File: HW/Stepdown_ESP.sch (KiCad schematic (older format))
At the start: 11 parts

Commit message: add some codes for JLCPCB, change package and schematic of CP2102
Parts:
- C? (x5): footprint Capacitor_SMD:C_1206_3216Metric -> Capacitor_SMD:C_0603_1608Metric; LCSC (none) -> C59461
- C?: LCSC (none) -> C1525
- C?: LCSC (none) -> C1567
- R?: LCSC (none) -> C25764
- U?: LCSC (none) -> C178247
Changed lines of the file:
@@
 F 0 "C?" H 4215 3646 50  0000 L CNN
 F 1 "22u" H 4215 3555 50  0000 L CNN
-F 2 "Capacitor_SMD:C_1206_3216Metric" H 4138 3450 50  0001 C CNN
+F 2 "Capacitor_SMD:C_0603_1608Metric" H 4138 3450 50  0001 C CNN
 F 3 "~" H 4100 3600 50  0001 C CNN
+F 4 "C59461" H 4100 3600 50  0001 C CNN "LCSC"
 	1    4100 3600
 	1    0    0    -1
@@
 F 0 "C?" H 4665 3646 50  0000 L CNN
 F 1 "22u" H 4665 3555 50  0000 L CNN
-F 2 "Capacitor_SMD:C_1206_3216Metric" H 4588 3450 50  0001 C CNN
+F 2 "Capacitor_SMD:C_0603_1608Metric" H 4588 3450 50  0001 C CNN
 F 3 "~" H 4550 3600 50  0001 C CNN
+F 4 "C59461" H 4550 3600 50  0001 C CNN "LCSC"
 	1    4550 3600
 	1    0    0    -1
@@
 F 0 "C?" H 5115 3646 50  0000 L CNN
 F 1 "22u" H 5115 3555 50  0000 L CNN
-F 2 "Capacitor_SMD:C_1206_3216Metric" H 5038 3450 50  0001 C CNN
+F 2 "Capacitor_SMD:C_0603_1608Metric" H 5038 3450 50  0001 C CNN
 F 3 "~" H 5000 3600 50  0001 C CNN
+F 4 "C59461" H 5000 3600 50  0001 C CNN "LCSC"
 	1    5000 3600
 	1    0    0    -1
@@
 F 2 "Resistor_SMD:R_0402_1005Metric" V 7380 3500 50  0001 C CNN
 F 3 "~" H 7450 3500 50  0001 C CNN
+F 4 "C25764" H 7450 3500 50  0001 C CNN "LCSC"
 	1    7450 3500
 	1    0    0    -1
@@
 F 2 "Capacitor_SMD:C_0402_1005Metric" H 6688 2750 50  0001 C CNN
 F 3 "~" H 6650 2900 50  0001 C CNN
+F 4 "C1525" H 6650 2900 50  0001 C CNN "LCSC"
 	1    6650 2900
 	0    1    1    0
@@
 F 2 "Capacitor_SMD:C_0402_1005Metric" H 8238 3400 50  0001 C CNN
 F 3 "~" H 8200 3550 50  0001 C CNN
+F 4 "C1567" H 8200 3550 50  0001 C CNN "LCSC"
 	1    8200 3550
 	-1   0    0    1
@@
 F 0 "C?" H 8585 3504 50  0000 R CNN
 F 1 "22u" H 8585 3595 50  0000 R CNN
-F 2 "Capacitor_SMD:C_1206_3216Metric" H 8738 3400 50  0001 C CNN
+F 2 "Capacitor_SMD:C_0603_1608Metric" H 8738 3400 50  0001 C CNN
 F 3 "~" H 8700 3550 50  0001 C CNN
+F 4 "C59461" H 8700 3550 50  0001 C CNN "LCSC"
 	1    8700 3550
 	-1   0    0    1
@@
 F 0 "C?" H 8935 3504 50  0000 R CNN
 F 1 "22u" H 8935 3595 50  0000 R CNN
-F 2 "Capacitor_SMD:C_1206_3216Metric" H 9088 3400 50  0001 C CNN
+F 2 "Capacitor_SMD:C_0603_1608Metric" H 9088 3400 50  0001 C CNN
 F 3 "~" H 9050 3550 50  0001 C CNN
+F 4 "C59461" H 9050 3550 50  0001 C CNN "LCSC"
 	1    9050 3550
 	-1   0    0    1
@@
 F 2 "Package_TO_SOT_SMD:TSOT-23-6" H 7050 3250 50  0001 C CNN
 F 3 "" H 6350 3600 50  0001 C CNN
+F 4 "C178247" H 6350 3600 50  0001 C CNN "LCSC"
 	1    6350 3600
 	1    0    0    -1

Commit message: add footprint of inductor, add codes for JLCPCB, repair mistakes
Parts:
- L?: footprint Inductor_SMD:L_0603_1608Metric -> my_library:MWSA0503S; LCSC (none) -> C408410
- R?: LCSC (none) -> C25895
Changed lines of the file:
@@
 F 2 "Resistor_SMD:R_0402_1005Metric" V 7380 4050 50  0001 C CNN
 F 3 "~" H 7450 4050 50  0001 C CNN
+F 4 "C25895" H 7450 4050 50  0001 C CNN "LCSC"
 	1    7450 4050
 	1    0    0    -1
@@
 F 0 "L?" V 7290 3300 50  0000 C CNN
 F 1 "4u7" V 7199 3300 50  0000 C CNN
-F 2 "Inductor_SMD:L_0603_1608Metric" H 7100 3300 50  0001 C CNN
+F 2 "my_library:MWSA0503S" H 7100 3300 50  0001 C CNN
 F 3 "~" H 7100 3300 50  0001 C CNN
+F 4 "C408410" H 7100 3300 50  0001 C CNN "LCSC"
 	1    7100 3300
 	0    -1   -1   0

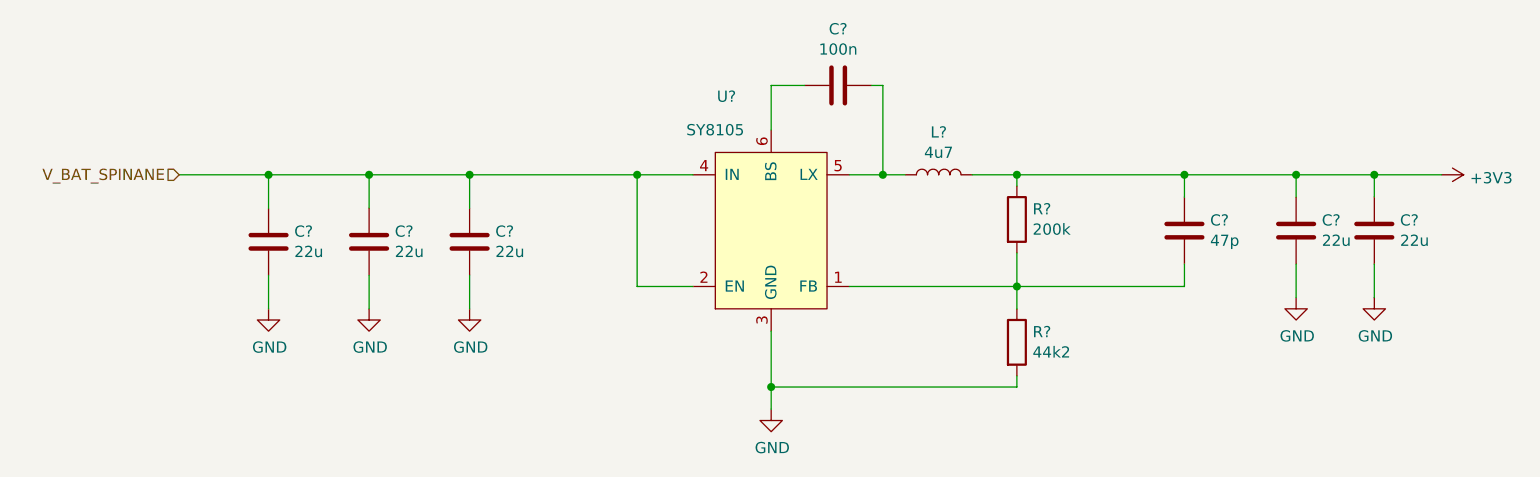
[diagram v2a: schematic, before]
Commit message: numbering components, place components on board
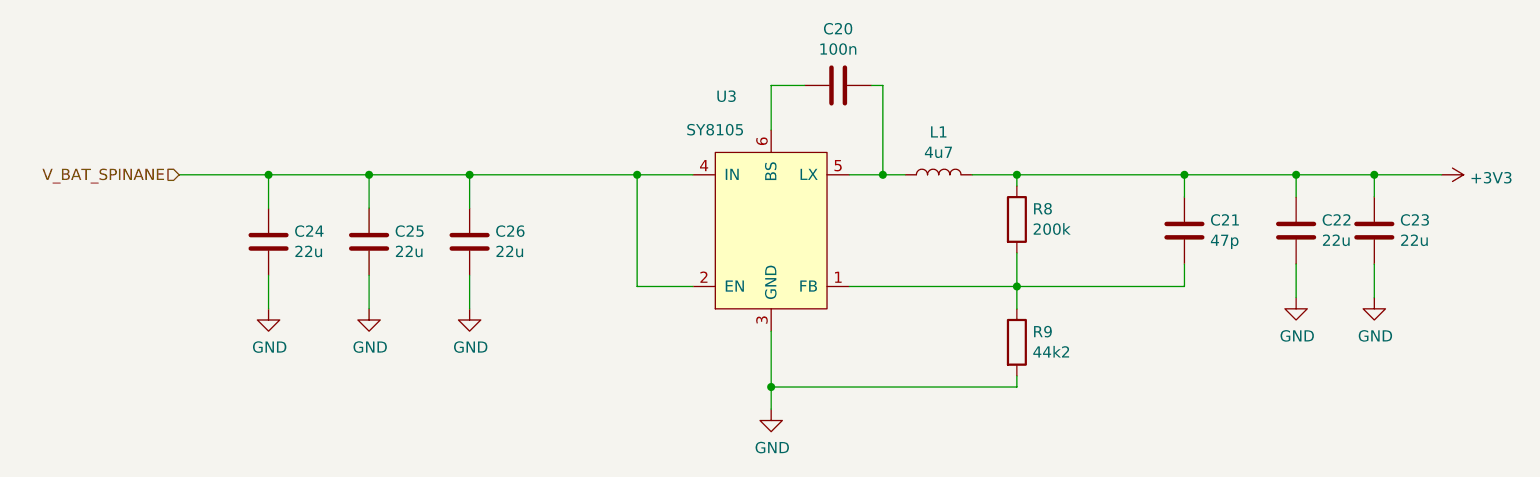
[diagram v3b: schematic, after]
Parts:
- gave numbers to parts that had none: 11
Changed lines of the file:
@@
 $EndDescr
 $Comp
-L Device:C C?
+L Device:C C24
 U 1 1 602B6CC6
 P 4100 3600
-F 0 "C?" H 4215 3646 50  0000 L CNN
+F 0 "C24" H 4215 3646 50  0000 L CNN
 F 1 "22u" H 4215 3555 50  0000 L CNN
 F 2 "Capacitor_SMD:C_0603_1608Metric" H 4138 3450 50  0001 C CNN
@@
 $EndComp
 $Comp
-L Device:C C?
+L Device:C C25
 U 1 1 602B7EED
 P 4550 3600
-F 0 "C?" H 4665 3646 50  0000 L CNN
+F 0 "C25" H 4665 3646 50  0000 L CNN
 F 1 "22u" H 4665 3555 50  0000 L CNN
 F 2 "Capacitor_SMD:C_0603_1608Metric" H 4588 3450 50  0001 C CNN
@@
 $EndComp
 $Comp
-L Device:C C?
+L Device:C C26
 U 1 1 602B82B1
 P 5000 3600
-F 0 "C?" H 5115 3646 50  0000 L CNN
+F 0 "C26" H 5115 3646 50  0000 L CNN
 F 1 "22u" H 5115 3555 50  0000 L CNN
 F 2 "Capacitor_SMD:C_0603_1608Metric" H 5038 3450 50  0001 C CNN
@@
 $EndComp
 $Comp
-L power:GND #PWR?
+L power:GND #PWR0133
 U 1 1 602B858C
 P 4100 3900
-F 0 "#PWR?" H 4100 3650 50  0001 C CNN
+F 0 "#PWR0133" H 4100 3650 50  0001 C CNN
 F 1 "GND" H 4105 3727 50  0000 C CNN
 F 2 "" H 4100 3900 50  0001 C CNN
@@
 $EndComp
 $Comp
-L power:GND #PWR?
+L power:GND #PWR0134
 U 1 1 602B8981
 P 4550 3900
-F 0 "#PWR?" H 4550 3650 50  0001 C CNN
+F 0 "#PWR0134" H 4550 3650 50  0001 C CNN
 F 1 "GND" H 4555 3727 50  0000 C CNN
 F 2 "" H 4550 3900 50  0001 C CNN
@@
 $EndComp
 $Comp
-L power:GND #PWR?
+L power:GND #PWR0135
 U 1 1 602B8C3F
 P 5000 3900
-F 0 "#PWR?" H 5000 3650 50  0001 C CNN
+F 0 "#PWR0135" H 5000 3650 50  0001 C CNN
 F 1 "GND" H 5005 3727 50  0000 C CNN
 F 2 "" H 5000 3900 50  0001 C CNN
@@
 Connection ~ 5000 3300
 $Comp
-L Device:R R?
+L Device:R R8
 U 1 1 602BA607
 P 7450 3500
-F 0 "R?" H 7520 3546 50  0000 L CNN
+F 0 "R8" H 7520 3546 50  0000 L CNN
 F 1 "200k" H 7520 3455 50  0000 L CNN
 F 2 "Resistor_SMD:R_0402_1005Metric" V 7380 3500 50  0001 C CNN
@@
 $EndComp
 $Comp
-L Device:R R?
+L Device:R R9
 U 1 1 602BAA94
 P 7450 4050
-F 0 "R?" H 7520 4096 50  0000 L CNN
+F 0 "R9" H 7520 4096 50  0000 L CNN
 F 1 "44k2" H 7520 4005 50  0000 L CNN
 F 2 "Resistor_SMD:R_0402_1005Metric" V 7380 4050 50  0001 C CNN
@@
 $EndComp
 $Comp
-L power:GND #PWR?
+L power:GND #PWR0136
 U 1 1 602BACDD
 P 6350 4350
-F 0 "#PWR?" H 6350 4100 50  0001 C CNN
+F 0 "#PWR0136" H 6350 4100 50  0001 C CNN
 F 1 "GND" H 6355 4177 50  0000 C CNN
 F 2 "" H 6350 4350 50  0001 C CNN
@@
 	7450 3900 7450 3800
 $Comp
-L Device:L L?
+L Device:L L1
 U 1 1 602BB352
 P 7100 3300
-F 0 "L?" V 7290 3300 50  0000 C CNN
+F 0 "L1" V 7290 3300 50  0000 C CNN
 F 1 "4u7" V 7199 3300 50  0000 C CNN
 F 2 "my_library:MWSA0503S" H 7100 3300 50  0001 C CNN
@@
 	7450 3300 7450 3350
 $Comp
-L Device:C C?
+L Device:C C20
 U 1 1 602BBFE2
 P 6650 2900
-F 0 "C?" V 6398 2900 50  0000 C CNN
+F 0 "C20" V 6398 2900 50  0000 C CNN
 F 1 "100n" V 6489 2900 50  0000 C CNN
 F 2 "Capacitor_SMD:C_0402_1005Metric" H 6688 2750 50  0001 C CNN
@@
 	6850 2900 6800 2900
 $Comp
-L Device:C C?
+L Device:C C21
 U 1 1 602BC82B
 P 8200 3550
-F 0 "C?" H 8085 3504 50  0000 R CNN
+F 0 "C21" H 8085 3504 50  0000 R CNN
 F 1 "47p" H 8085 3595 50  0000 R CNN
 F 2 "Capacitor_SMD:C_0402_1005Metric" H 8238 3400 50  0001 C CNN
@@
 $EndComp
 $Comp
-L Device:C C?
+L Device:C C22
 U 1 1 602BCF23
 P 8700 3550
-F 0 "C?" H 8585 3504 50  0000 R CNN
+F 0 "C22" H 8585 3504 50  0000 R CNN
 F 1 "22u" H 8585 3595 50  0000 R CNN
 F 2 "Capacitor_SMD:C_0603_1608Metric" H 8738 3400 50  0001 C CNN
@@
 $EndComp
 $Comp
-L Device:C C?
+L Device:C C23
 U 1 1 602BD148
 P 9050 3550
-F 0 "C?" H 8935 3504 50  0000 R CNN
+F 0 "C23" H 8935 3504 50  0000 R CNN
 F 1 "22u" H 8935 3595 50  0000 R CNN
 F 2 "Capacitor_SMD:C_0603_1608Metric" H 9088 3400 50  0001 C CNN
@@
 	7450 3800 7450 3650
 $Comp
-L power:GND #PWR?
+L power:GND #PWR0137
 U 1 1 602BE5D8
 P 8700 3850
-F 0 "#PWR?" H 8700 3600 50  0001 C CNN
+F 0 "#PWR0137" H 8700 3600 50  0001 C CNN
 F 1 "GND" H 8705 3677 50  0000 C CNN
 F 2 "" H 8700 3850 50  0001 C CNN
@@
 $EndComp
 $Comp
-L power:GND #PWR?
+L power:GND #PWR0138
 U 1 1 602BE8AF
 P 9050 3850
-F 0 "#PWR?" H 9050 3600 50  0001 C CNN
+F 0 "#PWR0138" H 9050 3600 50  0001 C CNN
 F 1 "GND" H 9055 3677 50  0000 C CNN
 F 2 "" H 9050 3850 50  0001 C CNN
@@
 	9050 3700 9050 3850
 $Comp
-L power:+3V3 #PWR?
+L power:+3V3 #PWR0139
 U 1 1 602BF312
 P 9350 3300
-F 0 "#PWR?" H 9350 3150 50  0001 C CNN
+F 0 "#PWR0139" H 9350 3150 50  0001 C CNN
 F 1 "+3V3" V 9365 3428 50  0000 L CNN
 F 2 "" H 9350 3300 50  0001 C CNN
@@
 $EndComp
 $Comp
-L symbols:SY8105 U?
+L symbols:SY8105 U3
 U 1 1 5F70D9AC
 P 6350 3600
-F 0 "U?" H 6150 4250 50  0000 C CNN
+F 0 "U3" H 6150 4250 50  0000 C CNN
 F 1 "SY8105" H 6100 4100 50  0000 C CNN
 F 2 "Package_TO_SOT_SMD:TSOT-23-6" H 7050 3250 50  0001 C CNN

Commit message: make smaller test version, start routing
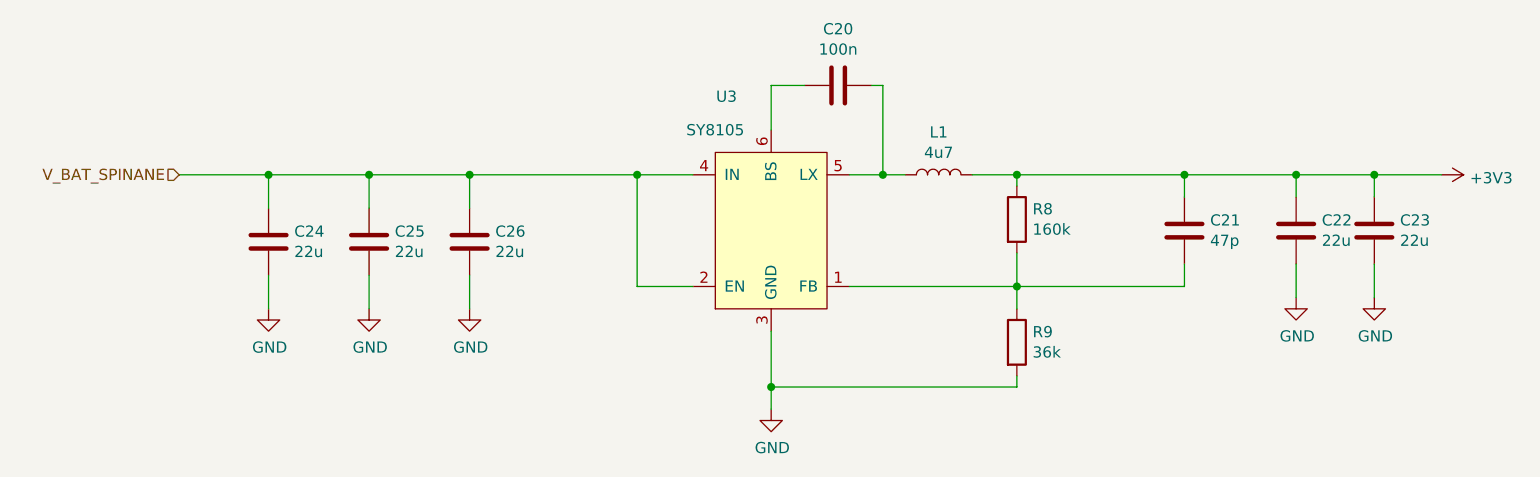
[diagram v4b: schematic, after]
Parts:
- R8: value 200k -> 160k; footprint Resistor_SMD:R_0402_1005Metric -> Resistor_SMD:R_0603_1608Metric; LCSC C25764 -> C22813
- R9: value 44k2 -> 36k; footprint Resistor_SMD:R_0402_1005Metric -> Resistor_SMD:R_0603_1608Metric; LCSC C25895 -> C23147
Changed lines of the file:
@@
 $Descr A4 11693 8268
 encoding utf-8
-Sheet 12 44
+Sheet 12 34
 Title ""
 Date ""
@@
 P 7450 3500
 F 0 "R8" H 7520 3546 50  0000 L CNN
-F 1 "200k" H 7520 3455 50  0000 L CNN
-F 2 "Resistor_SMD:R_0402_1005Metric" V 7380 3500 50  0001 C CNN
+F 1 "160k" H 7520 3455 50  0000 L CNN
+F 2 "Resistor_SMD:R_0603_1608Metric" V 7380 3500 50  0001 C CNN
 F 3 "~" H 7450 3500 50  0001 C CNN
-F 4 "C25764" H 7450 3500 50  0001 C CNN "LCSC"
+F 4 "C22813" H 7450 3500 50  0001 C CNN "LCSC"
 	1    7450 3500
 	1    0    0    -1
@@
 P 7450 4050
 F 0 "R9" H 7520 4096 50  0000 L CNN
-F 1 "44k2" H 7520 4005 50  0000 L CNN
-F 2 "Resistor_SMD:R_0402_1005Metric" V 7380 4050 50  0001 C CNN
+F 1 "36k" H 7520 4005 50  0000 L CNN
+F 2 "Resistor_SMD:R_0603_1608Metric" V 7380 4050 50  0001 C CNN
 F 3 "~" H 7450 4050 50  0001 C CNN
-F 4 "C25895" H 7450 4050 50  0001 C CNN "LCSC"
+F 4 "C23147" H 7450 4050 50  0001 C CNN "LCSC"
 	1    7450 4050
 	1    0    0    -1

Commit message: ready for first prototype
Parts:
- U3: JLCPCB_CORRECTION (none) -> 0;0;180
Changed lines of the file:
@@
 F 3 "" H 6350 3600 50  0001 C CNN
 F 4 "C178247" H 6350 3600 50  0001 C CNN "LCSC"
+F 5 "0;0;180" H 6350 3600 50  0001 C CNN "JLCPCB_CORRECTION"
 	1    6350 3600
 	1    0    0    -1
